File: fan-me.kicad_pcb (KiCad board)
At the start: 2 copper layers, 10 parts, among them CON1 BARREL_JACK, P1 CONN_01X04, SW1 SPST

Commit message: More tweaking
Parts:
- removed C1: 1u, Capacitors_SMD:C_0805
- removed C2: 2u2, Capacitors_SMD:C_0805
- removed P1: CONN_01X04, Pin_Headers:Pin_Header_Straight_1x04_Pitch2.54mm
- removed SW1: SPST, Pin_Headers:Pin_Header_Straight_1x03_Pitch1.00mm
- added J1: Conn_01x03, Connectors_Molex:Molex_KK-6410-03_03x2.54mm_Straight, F.Cu at (95.5, 53.0)
- added J2: Conn_01x03, Connectors_Molex:Molex_KK-6410-03_03x2.54mm_Straight, F.Cu at (95.5, 62.0)
- added Q1: BS107, TO_SOT_Packages_THT:TO-92_Molded_Narrow, F.Cu at (74.5, 45.0)
- added R4: 10k, Resistors_SMD:R_0805, B.Cu at (63.0, 45.0)
- added X1: PART, Mounting_Holes:MountingHole_3.2mm_M3, F.Cu at (85.0, 60.0)
- added X2: PART, Mounting_Holes:MountingHole_3.2mm_M3, F.Cu at (65.0, 60.0)
- R1, R2, R3: moved to B.Cu
- RV1: footprint Potentiometers:Potentiometer_Trimmer_Piher_PT-10v10_Horizontal_Px10.0mm_Py5.0mm_MountLS -> Potentiometers:Potentiometer_Trimmer_Piher_PT-10v10_Horizontal_Px10.0mm_Py5.0mm
- moved D1 53.8 mm to (81.0, 45.0)
- moved RV1 43.0 mm to (80.0, 53.0), turned to 180 degrees
- moved CON1 40.6 mm to (60.0, 55.0)
- moved R3 38.7 mm to (67.0, 45.0)
- moved R1 33.8 mm to (59.0, 45.0)
- moved R2 17.3 mm to (71.0, 45.0)
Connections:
- CON1 pad 1: Net-(CON1-Pad1) -> (no net)
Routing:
- added copper zone on F.Cu, net GND
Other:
- board outline added: 50 x 20 mm

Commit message: First pass board
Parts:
- removed Q1: BS107, TO_SOT_Packages_THT:TO-92_Molded_Narrow
- removed R2: 5k2, Resistors_SMD:R_0805
- added C1: 1u, agg:0805, B.Cu at (70.0, 63.0)
- added C2: 2u2, agg:0805, B.Cu at (80.0, 63.0)
- added SW1: SWITCH_SPDT, fan-me:A1xxxxCxxx, F.Cu at (75.0, 80.0)
- added U1: LDFPT-TR, fan-me:PPAK, B.Cu at (75.0, 65.8)
- added X1: PART, Mounting_Holes:MountingHole_3.2mm_M3, F.Cu at (96.0, 81.0)
- added X2: PART, Mounting_Holes:MountingHole_3.2mm_M3, F.Cu at (54.0, 81.0)
- D1: footprint LEDs:LED_0805 -> agg:0805-LED
- R1: footprint Resistors_SMD:R_0805 -> agg:0805
- R3: value 1k -> 30k; footprint Resistors_SMD:R_0805 -> agg:0805
- R4: value 10k -> 200k; footprint Resistors_SMD:R_0805 -> agg:0805
- RV1: value 6k -> 220k
- moved D1 27.0 mm to (66.0, 67.5), turned to 90 degrees
- moved R1 19.3 mm to (66.0, 63.0), turned to 270 degrees
- moved R4 18.4 mm to (77.0, 57.0), turned to 90 degrees
- moved R3 13.4 mm to (73.0, 57.0), turned to 90 degrees
- moved X1 12.5 mm to (96.0, 54.0)
- moved X2 12.5 mm to (54.0, 54.0)
- moved CON1 12.0 mm to (60.0, 67.0)
- moved RV1 11.7 mm to (70.0, 59.0), turned to 0 degrees
- moved J2 7.98 mm to (96.0, 69.9)
- moved J1 7.06 mm to (96.0, 60.0)
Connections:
- CON1 pad 1: (no net) -> Net-(CON1-Pad1)
- D1 pad 1: Net-(D1-Pad1) -> GND
- D1 pad 2: +12V -> Net-(D1-Pad2)
- J1 pad 2: VCC -> Net-(C2-Pad1)
- J2 pad 2: VCC -> Net-(C2-Pad1)
- R1 pad 1: Net-(D1-Pad1) -> +12V
- R1 pad 2: GND -> Net-(D1-Pad2)
- R4 pad 1: +12V -> Net-(C2-Pad1)
- R4 pad 2: (no net) -> Net-(R4-Pad2)
- RV1 pad 1: Net-(R2-Pad2) -> (no net)
- RV1 pad 2: Net-(R2-Pad2) -> Net-(R4-Pad2)
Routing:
- net Net-(C2-Pad1): track 0.00 -> 39.4 mm
- net +12V: track 0.00 -> 34.0 mm
- net Net-(CON1-Pad1): track 0.00 -> 25.8 mm
- net Net-(R3-Pad1): track 0.00 -> 20.5 mm
- net GND: track 0.00 -> 5.40 mm, vias 0 -> 10
- net Net-(R4-Pad2): track 0.00 -> 3.17 mm
- net Net-(D1-Pad2): track 0.00 -> 2.70 mm, vias 0 -> 1
- added copper zone on B.Cu, net GND
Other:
- board size 50 x 20 mm -> 50 x 35 mm
- net class Default: clearance 0 -> 0.25
- rule trace_clearance: 0 -> 0.25

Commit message: Tweaked first board version
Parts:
- removed X1 (x2), X2 (x2): PART, Mounting_Holes:MountingHole_3.2mm_M3
- added REF**: MountingHole_3.2mm_M3, Mounting_Holes:MountingHole_3.2mm_M3, F.Cu at (96.0, 81.0)
- added REF**: MountingHole_3.2mm_M3, Mounting_Holes:MountingHole_3.2mm_M3, F.Cu at (54.0, 81.0)
- added REF**: MountingHole_3.2mm_M3, Mounting_Holes:MountingHole_3.2mm_M3, F.Cu at (54.0, 54.0)
- added REF**: MountingHole_3.2mm_M3, Mounting_Holes:MountingHole_3.2mm_M3, F.Cu at (96.0, 54.0)
- J1: value Conn_01x03 -> FAN2
- J2: value Conn_01x03 -> FAN1
- ON: renamed from SW1; value SWITCH_SPDT -> OFF
- renumbered D1 to PWR
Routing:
- net GND: track 5.40 -> 3.20 mm

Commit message: Mk2 board 30x50
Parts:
- removed the REF** at (96.0, 81.0)
- removed the REF** at (54.0, 81.0)
- moved ON 25.0 mm to (75.0, 55.0)
- moved R3 16.0 mm to (77.0, 72.5), turned to 270 degrees
- moved R4 16.0 mm to (73.0, 72.5), turned to 270 degrees
- moved RV1 15.2 mm to (80.0, 70.5), turned to 180 degrees
- moved CON1 12.2 mm to (62.0, 55.0)
- moved REF** 11.0 mm to (55.0, 65.0)
- moved REF** 11.0 mm to (95.0, 65.0)
- moved C1 8.39 mm to (77.5, 59.2), turned to 0 degrees
- moved J1 6.54 mm to (96.0, 53.5)
- moved C2 4.84 mm to (82.5, 67.2)
- moved U1 2.78 mm to (77.7, 65.0), turned to 270 degrees
- moved PWR 2.69 mm to (65.0, 65.0)
- moved R1 2.69 mm to (65.0, 60.5)
- moved J2 1.54 mm to (96.0, 71.5)
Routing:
- net Net-(CON1-Pad1): track 25.8 -> 0.00 mm
- net Net-(R3-Pad1): track 20.5 -> 10.9 mm
- net +12V: track 34.0 -> 26.2 mm
- net Net-(C2-Pad1): track 39.4 -> 46.6 mm
- net GND: track 3.20 -> 0.00 mm, vias 10 -> 9
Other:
- board size 50 x 35 mm -> 50 x 30 mm

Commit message: Board smollification mk3
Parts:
- REF** (x2): footprint Mounting_Holes:MountingHole_3.2mm_M3 -> Mounting_Holes:MountingHole_2.7mm_M2.5
- moved ON 22.3 mm to (53.2, 60.0), turned to 180 degrees
- moved R4 18.6 mm to (90.0, 64.8), turned to 90 degrees
- moved C1 11.9 mm to (87.9, 53.4)
- moved PWR 11.4 mm to (70.0, 54.8), turned to 180 degrees
- moved U1 10.3 mm to (82.5, 55.9)
- moved R3 10.1 mm to (79.8, 62.8)
- moved J2 9.04 mm to (95.8, 62.4)
- moved CON1 7.65 mm to (68.0, 59.8), turned to 90 degrees
- moved REF** 7.07 mm to (90.0, 60.0)
- moved REF** 7.07 mm to (60.0, 60.0)
- moved C2 6.41 mm to (85.0, 61.2), turned to 180 degrees
- moved R1 5.94 mm to (66.5, 54.8), turned to 0 degrees
- moved RV1 4.89 mm to (76.8, 66.8), turned to 0 degrees
- moved J1 0.97 mm to (95.9, 52.5)
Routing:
- net +12V: track 26.2 -> 47.6 mm
- net Net-(CON1-Pad1): track 0.00 -> 17.8 mm
- net Net-(C2-Pad1): track 46.6 -> 38.4 mm
- net GND: track 0.00 -> 3.77 mm, vias 9 -> 12
- net Net-(D1-Pad2): track 2.70 -> 1.70 mm
- net Net-(R3-Pad1): track 10.9 -> 10.0 mm
- removed copper zone on B.Cu, net GND
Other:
- board size 50 x 30 mm -> 50 x 20 mm

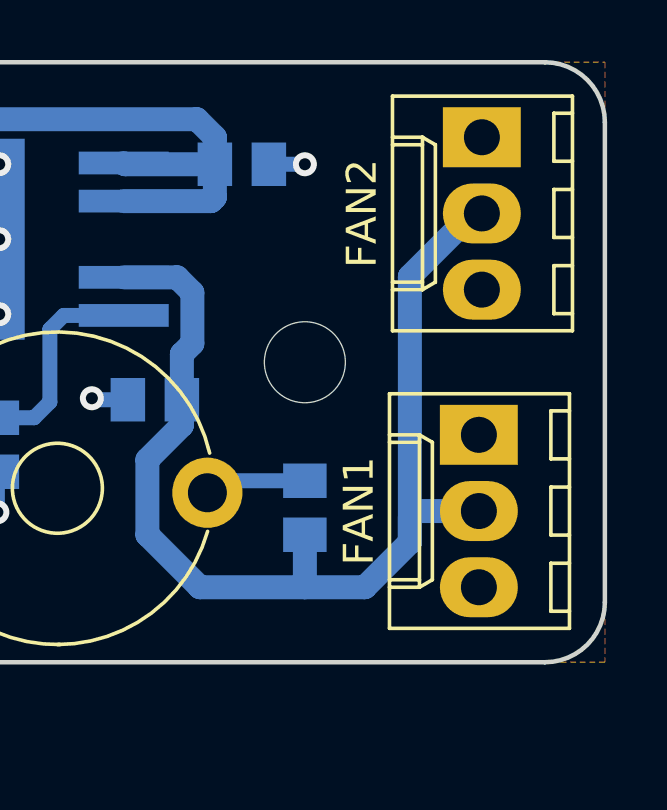
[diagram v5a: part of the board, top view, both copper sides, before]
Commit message: Add proper footprint for fan connectors
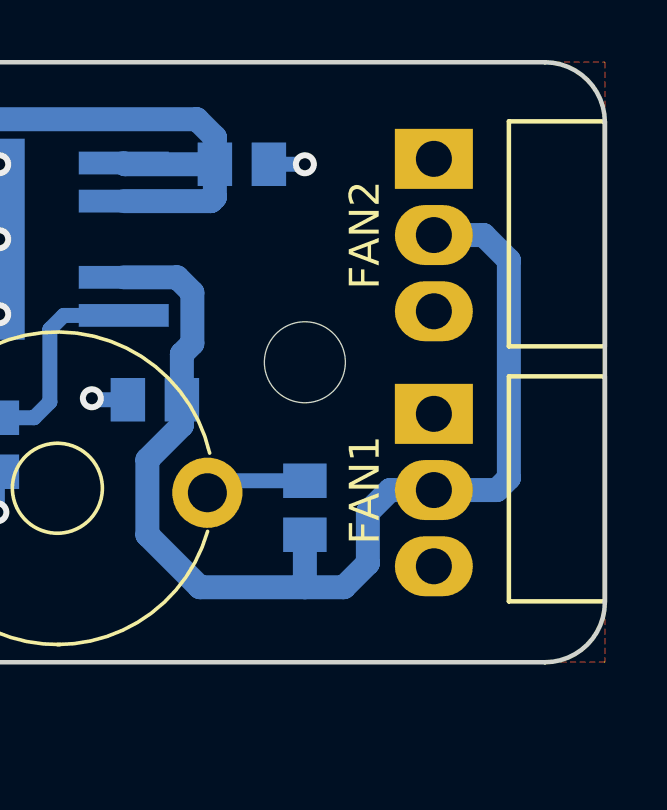
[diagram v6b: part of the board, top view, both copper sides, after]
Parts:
- J1, J2: footprint Connectors_Molex:Molex_KK-6410-03_03x2.54mm_Straight -> fan-me:Molex_KK-6410-03_03x2.54mm_Angle
- moved J1 1.75 mm to (94.3, 53.2)
- moved J2 1.66 mm to (94.3, 61.7)

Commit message: Further tweaks ready for V1 boards
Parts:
- removed REF** (x2): MountingHole_3.2mm_M3, Mounting_Holes:MountingHole_2.7mm_M2.5
- added X1: , Mounting_Holes:MountingHole_2.7mm_M2.5, F.Cu at (60.0, 60.0)
- added X2: , Mounting_Holes:MountingHole_2.7mm_M2.5, F.Cu at (90.0, 60.0)
- C1, C2, R1, R3, R4: footprint agg:0805 -> agg:0603
- D1: renamed from PWR; value Led_Small -> PWR
- J1: value FAN2 -> FAN1
- J2: value FAN1 -> FAN2
- SW1: renamed from ON; value OFF -> (none)
- moved R4 6.02 mm to (85.0, 61.5), turned to 270 degrees
- moved C2 5.83 mm to (88.0, 56.2), turned to 0 degrees
- moved R1 5.26 mm to (71.8, 55.0), turned to 270 degrees
- moved D1 1.77 mm to (71.8, 55.0), turned to 270 degrees
- moved C1 0.18 mm to (88.0, 53.2)
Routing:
- net Net-(C2-Pad1): track 38.3 -> 29.9 mm
- net Net-(D1-Pad2): track 1.70 -> 0.00 mm
- net +12V: track 47.6 -> 46.5 mm
- net Net-(R4-Pad2): track 3.42 -> 2.77 mm
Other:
- board text added: "12v DC"
- board text added: "OFF"
- board text added: "ON"
